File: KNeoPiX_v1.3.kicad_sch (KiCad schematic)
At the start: 30 parts, among them J1 Conn_KNX, J2 Conn_KNX, J3 Screw Terminal - Non Isolated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, J4 Screw Terminal - Isolated IOs, SW1 Prog BTN, U1 Seeeduino XIAO, U2 LM2937IMP-3.3 / 5.0, U3 ADuM1201AR / ADum1250, U4 ADuM1201AR / ADum1250

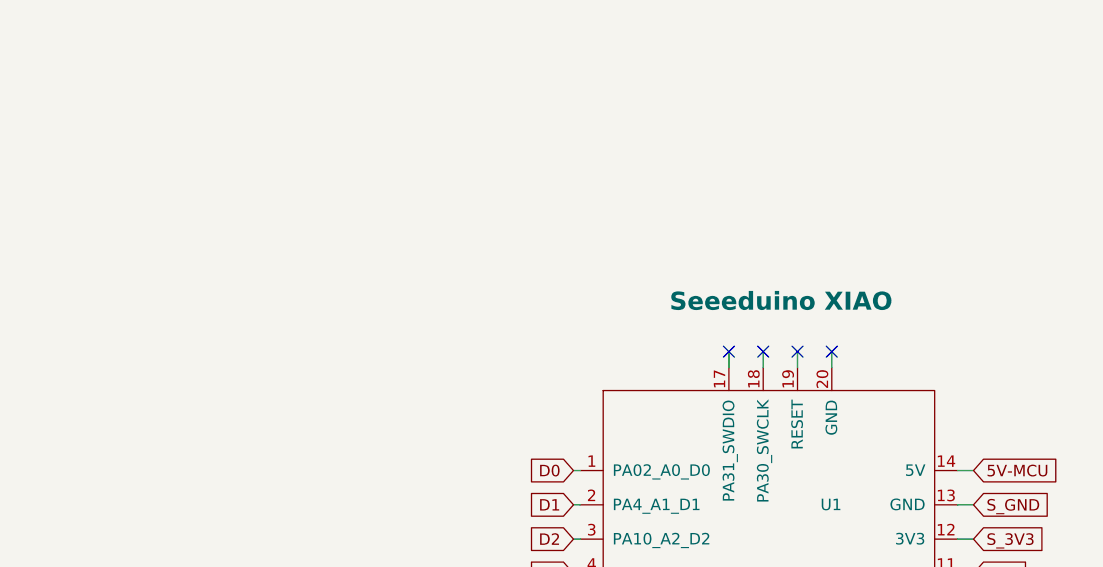
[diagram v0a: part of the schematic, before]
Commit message: WIP - After Migration to KiCad 7
Add. 4 Layer
Add. DebugInterface
Add. Solder Cuts for XIAO - Reset, SWDIO, SWCLK
New order of all footprints and also rerouting then.
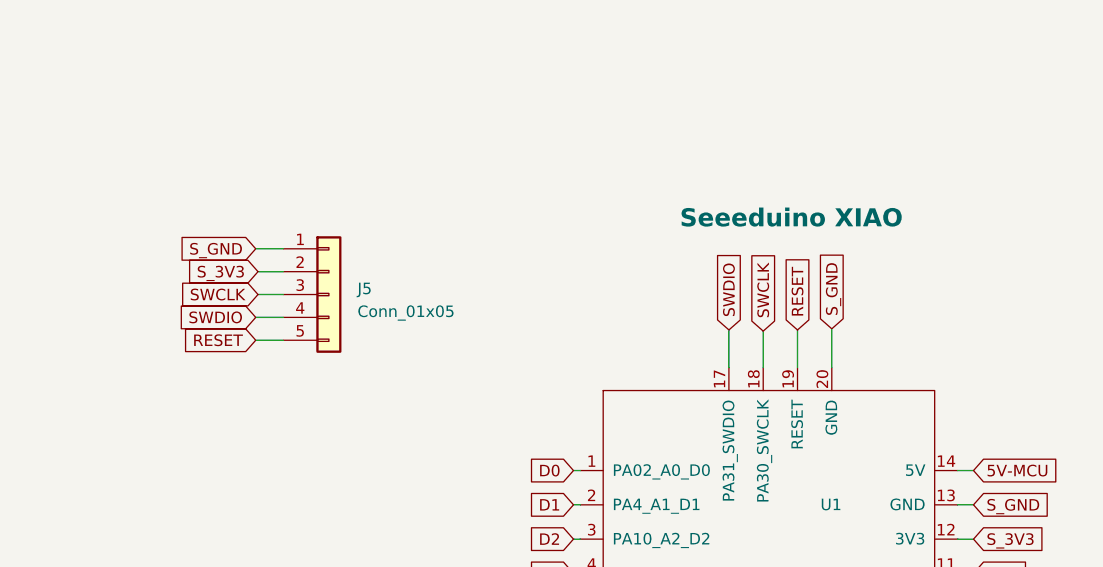
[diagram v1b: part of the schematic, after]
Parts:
- added J5: Conn_01x05, Connector_PinHeader_1.27mm:PinHeader_1x05_P1.27mm_Vertical, symbol Connector_Generic:Conn_01x05
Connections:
- net EXT_GND: now also U1.20 (GND), J5.1 (Pin_1)
- net S_3V3: now also J5.2 (Pin_2)
- net SWDIO: now reaches U1.17 (PA31_SWDIO)
- net SWDIO: now also J5.4 (Pin_4)
- net SWCLK: now reaches U1.18 (PA30_SWCLK)
- net SWCLK: now also J5.3 (Pin_3)
- net RESET: now reaches U1.19 (RESET)
- net RESET: now also J5.5 (Pin_5)
- no-connect marks 6 -> 2
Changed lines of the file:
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@@
   (junction (at 44.831 240.284) (diameter 0) (color 0 0 0 0)
   )
-  (no_connect (at 307.594 130.048))
-  (no_connect (at 311.404 130.048))
-  (no_connect (at 315.214 130.048))
-  (no_connect (at 319.024 130.048))
   (no_connect (at 310.134 178.054))
   (no_connect (at 315.214 178.054))
@@
     (stroke (width 0) (type default))
   )
+  (wire (pts (xy 255.016 128.778) (xy 258.064 128.778))
+    (stroke (width 0) (type default))
+  )
   (wire (pts (xy 77.851 249.936) (xy 77.851 247.904))
+    (stroke (width 0) (type default))
+  )
+  (wire (pts (xy 307.594 127.635) (xy 307.594 131.826))
     (stroke (width 0) (type default))
   )
@@
     (stroke (width 0) (type default))
   )
-  (wire (pts (xy 307.594 131.826) (xy 307.594 130.048))
-    (stroke (width 0) (type default))
-  )
   (wire (pts (xy 273.812 195.834) (xy 268.478 195.834))
     (stroke (width 0) (type default))
@@
     (stroke (width 0) (type default))
   )
+  (wire (pts (xy 319.024 127.508) (xy 319.024 131.826))
+    (stroke (width 0) (type default))
+  )
   (polyline (pts (xy 398.78 168.656) (xy 398.526 197.358))
     (stroke (width 0.25) (type dot))
@@
     (stroke (width 0.25) (type dot) (color 0 0 255 1))
   )
+  (wire (pts (xy 255.016 126.238) (xy 258.064 126.238))
+    (stroke (width 0) (type default))
+  )
   (wire (pts (xy 290.322 150.876) (xy 291.084 150.876))
     (stroke (width 0) (type default))
@@
     (stroke (width 0) (type default))
   )
+  (wire (pts (xy 255.27 123.698) (xy 258.064 123.698))
+    (stroke (width 0) (type default))
+  )
   (wire (pts (xy 273.812 191.516) (xy 273.812 195.834))
     (stroke (width 0) (type default))
   )
+  (wire (pts (xy 311.404 127.762) (xy 311.404 131.826))
+    (stroke (width 0) (type default))
+  )
   (polyline (pts (xy 253.238 85.344) (xy 253.238 23.622))
     (stroke (width 0) (type default))
@@
     (stroke (width 0) (type default))
   )
+  (wire (pts (xy 255.27 121.158) (xy 258.064 121.158))
+    (stroke (width 0) (type default))
+  )
   (polyline (pts (xy 206.502 121.666) (xy 206.502 191.77))
     (stroke (width 0) (type default))
   )
+  (wire (pts (xy 315.214 127.635) (xy 315.214 131.826))
+    (stroke (width 0) (type default))
+  )
   (polyline (pts (xy 154.686 130.302) (xy 154.686 151.892))
     (stroke (width 0.25) (type dot) (color 0 0 255 1))
@@
   )
   (wire (pts (xy 198.374 39.878) (xy 210.566 39.878))
-    (stroke (width 0) (type default))
-  )
-  (wire (pts (xy 315.214 131.826) (xy 315.214 130.048))
     (stroke (width 0) (type default))
   )
@@
     (stroke (width 0) (type default))
   )
+  (wire (pts (xy 255.016 118.618) (xy 258.064 118.618))
+    (stroke (width 0) (type default))
+  )
   (polyline (pts (xy 116.332 162.814) (xy 150.876 162.814))
     (stroke (width 0.25) (type dot) (color 0 0 255 1))
@@
     (stroke (width 0.25) (type dot) (color 0 0 255 1))
   )
-  (wire (pts (xy 311.404 130.048) (xy 311.404 131.826))
-    (stroke (width 0) (type default))
-  )
   (wire (pts (xy 334.772 166.116) (xy 332.994 166.116))
     (stroke (width 0) (type default))
@@
   (polyline (pts (xy 145.669 208.534) (xy 180.213 208.534))
     (stroke (width 0.25) (type dot) (color 0 0 255 1))
-  )
-  (wire (pts (xy 319.024 130.048) (xy 319.024 131.826))
-    (stroke (width 0) (type default))
   )
   (wire (pts (xy 383.032 81.28) (xy 383.032 79.756))
@@
     )
   )
+  (global_label "SWCLK" (shape input) (at 255.27 123.698 180) (fields_autoplaced)
+    (effects (font (size 1.27 1.27)) (justify right))
+    (property "Intersheetrefs" "${INTERSHEET_REFS}" (at 246.1352 123.698 0)
+      (effects (font (size 1.27 1.27)) (justify right) hide)
+    )
+  )
   (global_label "D6_TX" (shape input) (at 290.322 166.116 180) (fields_autoplaced)
     (effects (font (size 1.27 1.27)) (justify right))
@@
     )
   )
+  (global_label "S_3V3" (shape input) (at 255.27 121.158 180) (fields_autoplaced)
+    (effects (font (size 1.27 1.27)) (justify right))
+    (property "Intersheetrefs" "${INTERSHEET_REFS}" (at 246.6795 121.158 0)
+      (effects (font (size 1.27 1.27)) (justify right) hide)
+    )
+  )
   (global_label "S_GND" (shape input) (at 334.772 147.066 0) (fields_autoplaced)
     (effects (font (size 1.27 1.27)) (justify left))
@@
     )
   )
+  (global_label "SWCLK" (shape input) (at 311.404 127.762 90) (fields_autoplaced)
+    (effects (font (size 1.27 1.27)) (justify left))
+    (property "Intersheetrefs" "${INTERSHEET_REFS}" (at 311.404 118.6272 90)
+      (effects (font (size 1.27 1.27)) (justify left) hide)
+    )
+  )
+  (global_label "S_GND" (shape input) (at 319.024 127.508 90) (fields_autoplaced)
+    (effects (font (size 1.27 1.27)) (justify left))
+    (property "Intersheetrefs" "${INTERSHEET_REFS}" (at 319.024 118.5546 90)
+      (effects (font (size 1.27 1.27)) (justify left) hide)
+    )
+  )
   (global_label "KNX_5V" (shape input) (at 80.772 133.096 180) (fields_autoplaced)
     (effects (font (size 1.27 1.27)) (justify right))
@@
     )
   )
+  (global_label "RESET" (shape input) (at 315.214 127.635 90) (fields_autoplaced)
+    (effects (font (size 1.27 1.27)) (justify left))
+    (property "Intersheetrefs" "${INTERSHEET_REFS}" (at 315.214 118.9841 90)
+      (effects (font (size 1.27 1.27)) (justify left) hide)
+    )
+  )
   (global_label "D7_RX" (shape input) (at 86.614 102.616 0) (fields_autoplaced)
     (effects (font (size 1.27 1.27)) (justify left))
@@
     )
   )
+  (global_label "RESET" (shape input) (at 255.016 128.778 180) (fields_autoplaced)
+    (effects (font (size 1.27 1.27)) (justify right))
+    (property "Intersheetrefs" "${INTERSHEET_REFS}" (at 246.3651 128.778 0)
+      (effects (font (size 1.27 1.27)) (justify right) hide)
+    )
+  )
   (global_label "KNX+" (shape input) (at 97.282 51.816 0) (fields_autoplaced)
     (effects (font (size 1.27 1.27)) (justify left))
@@
     )
   )
+  (global_label "SWDIO" (shape input) (at 307.594 127.635 90) (fields_autoplaced)
+    (effects (font (size 1.27 1.27)) (justify left))
+    (property "Intersheetrefs" "${INTERSHEET_REFS}" (at 307.594 118.863 90)
+      (effects (font (size 1.27 1.27)) (justify left) hide)
+    )
+  )
   (global_label "KNX_5V" (shape input) (at 37.338 53.086 0) (fields_autoplaced)
     (effects (font (size 1.27 1.27)) (justify left))
@@
     )
   )
+  (global_label "SWDIO" (shape input) (at 255.016 126.238 180) (fields_autoplaced)
+    (effects (font (size 1.27 1.27)) (justify right))
+    (property "Intersheetrefs" "${INTERSHEET_REFS}" (at 246.244 126.238 0)
+      (effects (font (size 1.27 1.27)) (justify right) hide)
+    )
+  )
   (global_label "S_GND" (shape input) (at 153.67 61.722 180) (fields_autoplaced)
     (effects (font (size 1.27 1.27)) (justify right))
@@
     (effects (font (size 1.27 1.27)) (justify right))
     (property "Intersheetrefs" "${INTERSHEET_REFS}" (at 164.4528 73.3266 0)
+      (effects (font (size 1.27 1.27)) (justify right) hide)
+    )
+  )
+  (global_label "S_GND" (shape input) (at 255.016 118.618 180) (fields_autoplaced)
+    (effects (font (size 1.27 1.27)) (justify right))
+    (property "Intersheetrefs" "${INTERSHEET_REFS}" (at 246.0626 118.618 0)
       (effects (font (size 1.27 1.27)) (justify right) hide)
     )
@@
       (effects (font (size 1.27 1.27)) (justify left))
     )
-    (property "Value" "Seeeduino XIAO" (at 300.99 124.46 0)
+    (property "Value" "Seeeduino XIAO" (at 302.133 115.189 0)
       (effects (font (size 2 2) bold) (justify left))
     )
@@
         )
       )
+    )
+  )
+  (symbol (lib_id "Connector_Generic:Conn_01x05") (at 263.144 123.698 0) (unit 1)
+    (in_bom yes) (on_board yes) (dnp no) (fields_autoplaced)
+    (property "Reference" "J5" (at 266.319 123.063 0)
+      (effects (font (size 1.27 1.27)) (justify left))
+    )
+    (property "Value" "Conn_01x05" (at 266.319 125.603 0)
+      (effects (font (size 1.27 1.27)) (justify left))
+    )
+    (property "Footprint" "Connector_PinHeader_1.27mm:PinHeader_1x05_P1.27mm_Vertical" (at 263.144 123.698 0)
+      (effects (font (size 1.27 1.27)) hide)
+    )
+    (property "Datasheet" "~" (at 263.144 123.698 0)
+      (effects (font (size 1.27 1.27)) hide)
+    )
+    (pin "1")
+    (pin "2")
+    (pin "3")
+    (pin "4")
+    (pin "5")
+    (instances
+      (project "KNeoPiX_v1.3"
+        (path "/e63e39d7-6ac0-4ffd-8aa3-1841a4541b55"
+          (reference "J5") (unit 1)
+        )
+      )

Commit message: Pre-Ready for  1st Prod. Needs to be checked again.
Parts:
- added J6: Conn_01x05, Connector_PinHeader_1.00mm:PinHeader_1x05_P1.00mm_Vertical, symbol Connector_Generic:Conn_01x05
- C1, C2, C3, C4, C5, C6, C7: footprint Capacitor_SMD:C_0805_2012Metric -> KNeoPix:C_0805_2012Metric
- D3: footprint Diode_SMD:D_SMA -> KNeoPix:D_SMA
- GN1: footprint OpenKNX:NanoBCU_PinSocket_LowProfile -> KNeoPix:NanoBCU_PinSocket_LowProfile
- H1, H2: footprint WAGO-243-131:243131 -> KNeoPix:243131
- J1: footprint OpenKNX:KNX_Connector -> KNeoPix:KNX_Connector
- J2: footprint OpenKNX:KNX_Connector_Light -> KNeoPix:KNX_Connector_Light
- J3: footprint TerminalBlock_Phoenix:TerminalBlock_Phoenix_MPT-0,5-9-2.54_1x09_P2.54mm_Horizontal -> KNeoPix:TerminalBlock_Phoenix_MPT-0,5-9-2.54_1x09_P2.54mm_Horizontal
- J4: footprint TerminalBlock_Phoenix:TerminalBlock_Phoenix_MPT-0,5-4-2.54_1x04_P2.54mm_Horizontal -> KNeoPix:TerminalBlock_Phoenix_MPT-0,5-4-2.54_1x04_P2.54mm_Horizontal
- J5: footprint Connector_PinHeader_1.27mm:PinHeader_1x05_P1.27mm_Vertical -> Connector_JST:JST_SH_BM05B-SRSS-TB_1x05-1MP_P1.00mm_Vertical
- JP1, JP2, JP3, JP4, JP6: footprint Jumper:SolderJumper-2_P1.3mm_Open_Pad1.0x1.5mm -> KNeoPix:SolderJumper-2_P1.3mm_Open_Pad1.0x1.5mm
- JP5: footprint Jumper:SolderJumper-3_P1.3mm_Open_RoundedPad1.0x1.5mm -> KNeoPix:SolderJumper-3_P1.3mm_Open_RoundedPad1.0x1.5mm
- R1, R2, R3, R4: footprint Resistor_SMD:R_0402_1005Metric_Pad0.72x0.64mm_HandSolder -> KNeoPix:R_0402_1005Metric_Pad0.72x0.64mm_HandSolder
- SW1: footprint Button_Switch_SMD:SW_Push_1P1T_NO_CK_KMR2 -> KNeoPix:SW_Push_1P1T_NO_CK_KMR2
- U1: footprint OpenKNX:Seeeduino XIAO-MOUDLE14P-2.54-21X17.8MM-no-15-16-17-18-19-20-pad -> KNeoPix:Seeeduino XIAO-MOUDLE14P-2.54-21X17.8MM-no-15-16-17-18-19-20-pad
- U2: footprint Package_TO_SOT_SMD:SOT-223-3_TabPin2 -> KNeoPix:SOT-223-3_TabPin2
- U3: footprint Package_SO:SOIC-8_3.9x4.9mm_P1.27mm -> KNeoPix:SOIC-8_3.9x4.9mm_P1.27mm
- U4: value ADuM1201AR / ADum1250 -> ADum1250; footprint Package_SO:SOIC-8_3.9x4.9mm_P1.27mm -> KNeoPix:SOIC-8_3.9x4.9mm_P1.27mm
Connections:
- net EXT_GND: now also J6.1 (Pin_1)
- net RESET: now also J6.5 (Pin_5)
- net SWCLK: now also J6.3 (Pin_3)
- net SWDIO: now also J6.4 (Pin_4)
- net S_3V3: now also J6.2 (Pin_2)

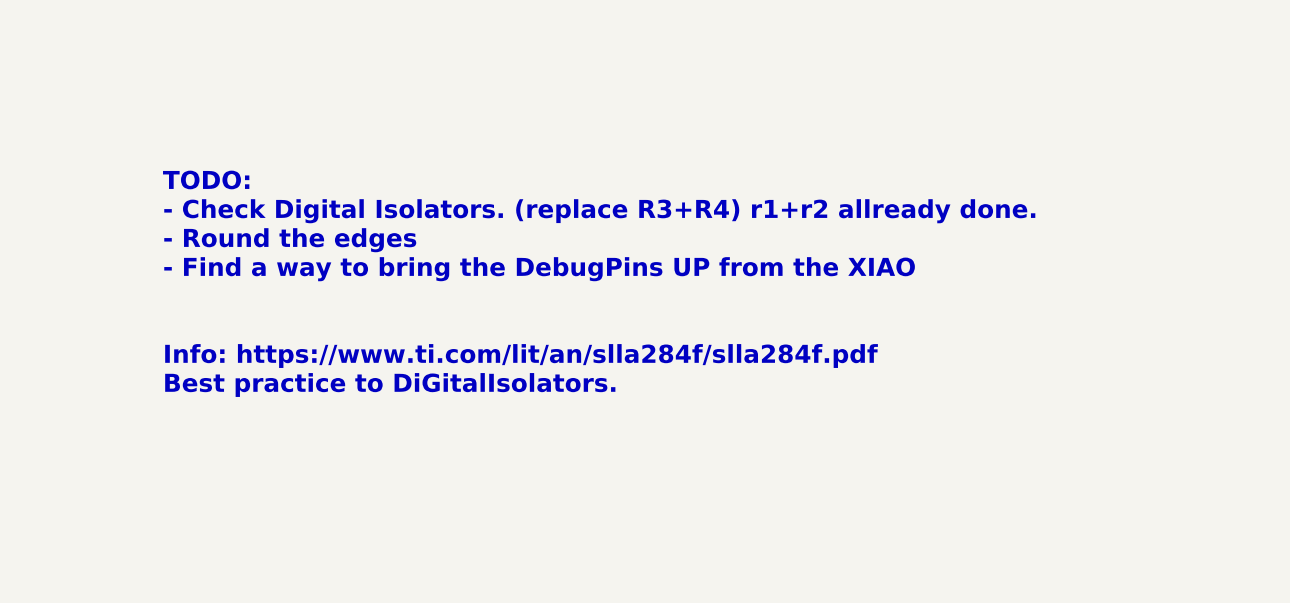
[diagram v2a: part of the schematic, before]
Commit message: Finalized version v1.3!
Every is now checked and Ready for 1st pcb production!
Next todo is to clean up the whole project, files, folders, footprint and also the 3d files.
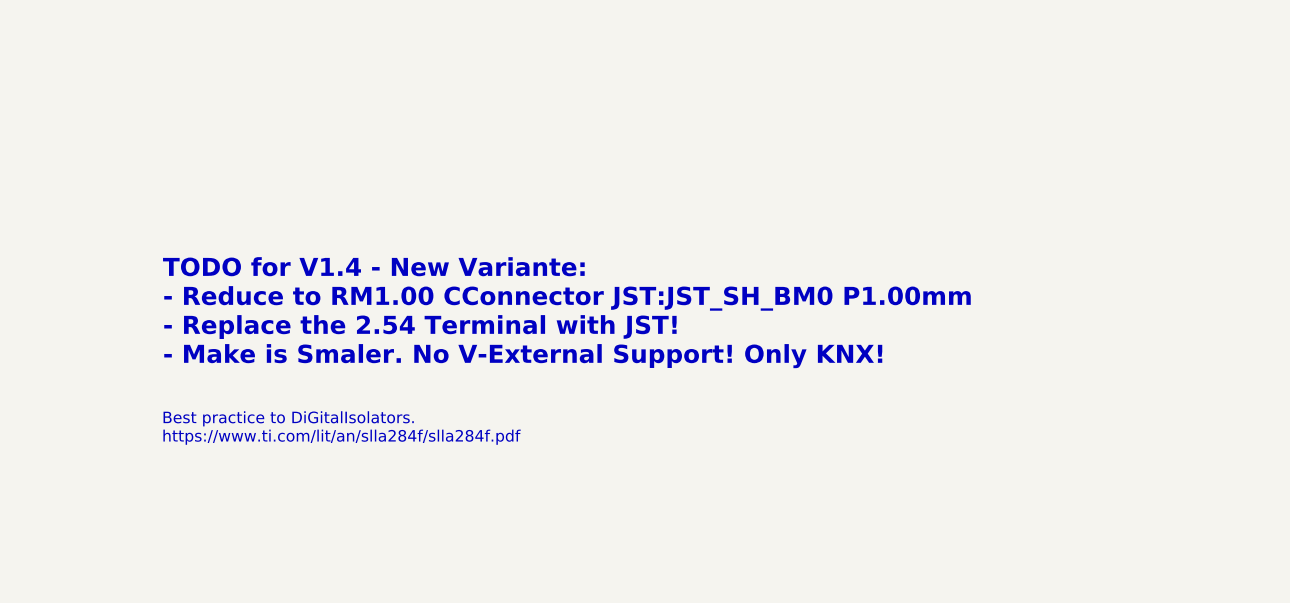
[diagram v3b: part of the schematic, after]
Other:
- note added: "Best practice to DiGitalIsolators. https://www.ti.com/lit/an/slla284f/slla284f.pdf"
- note added: "TODO for V1.4 - New Variante: - Reduce to RM1.00 CConnector JST:JST_SH_BM0 P1.00mm - Replace the 2.54 Terminal with JST! - Make is Smaler. No V-External Support! Only KNX!"
- note removed: "TODO: - Check Digital Isolators. (replace R3+R4) r1+r2 allready done. - Round the edges - Find a way to bring the DebugPins UP from the XIAO Info: https://www.ti.com/lit/an/slla284f/slla284f.pdf Best practice to DiGitalIsolators."
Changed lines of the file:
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@@
     (effects (font (size 1.27 1.27)) (justify left bottom))
   )
-  (text "TODO:\n- Check Digital Isolators. (replace R3+R4) r1+r2 allready done. \n- Round the edges\n- Find a way to bring the DebugPins UP from the XIAO\n\n\nInfo: https://www.ti.com/lit/an/slla284f/slla284f.pdf\nBest practice to DiGitalIsolators."
+  (text "TODO for V1.4 - New Variante: \n- Reduce to RM1.00 CConnector JST:JST_SH_BM0 P1.00mm\n- Replace the 2.54 Terminal with JST!\n- Make is Smaler. No V-External Support! Only KNX!\n\n"
     (at 298.8056 242.2144 0)
     (effects (font (size 2 2) bold) (justify left bottom))
@@
     (effects (font (size 1.27 1.27)) (justify left bottom))
   )
+  (text "Best practice to DiGitalIsolators.\nhttps://www.ti.com/lit/an/slla284f/slla284f.pdf\n"
+    (at 298.704 247.65 0)
+    (effects (font (size 1.27 1.27)) (justify left bottom) (href "https://www.ti.com/lit/an/slla284f/slla284f.pdf"))
+  )
   (text "External 5V ONLY:" (at 154.432 168.402 0)
